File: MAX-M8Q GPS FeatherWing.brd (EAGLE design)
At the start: 50.8 x 22.9 mm, 28 parts, among them Q1 DMG3415U-7, Q2 2N2222, SW1 KMR2, X1 uFL

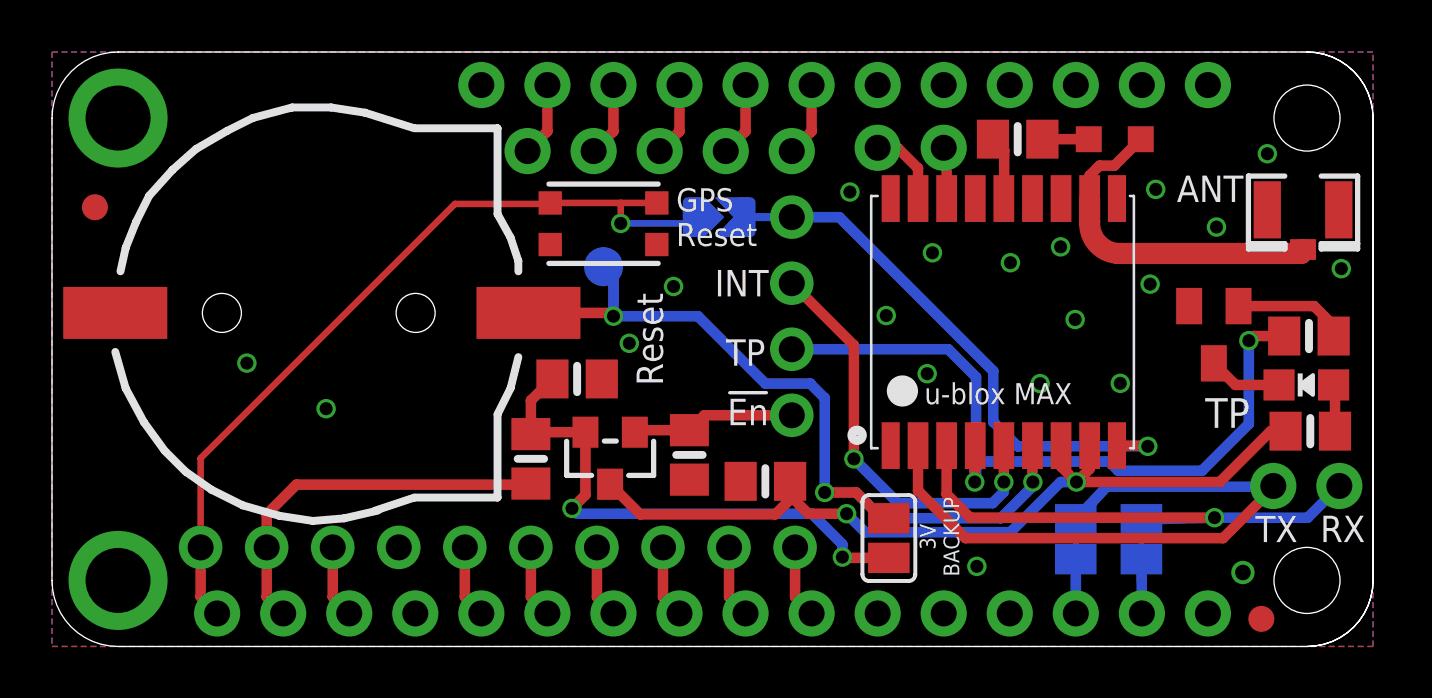
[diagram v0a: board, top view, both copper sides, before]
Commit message: Minor tweaks. Included BOM.
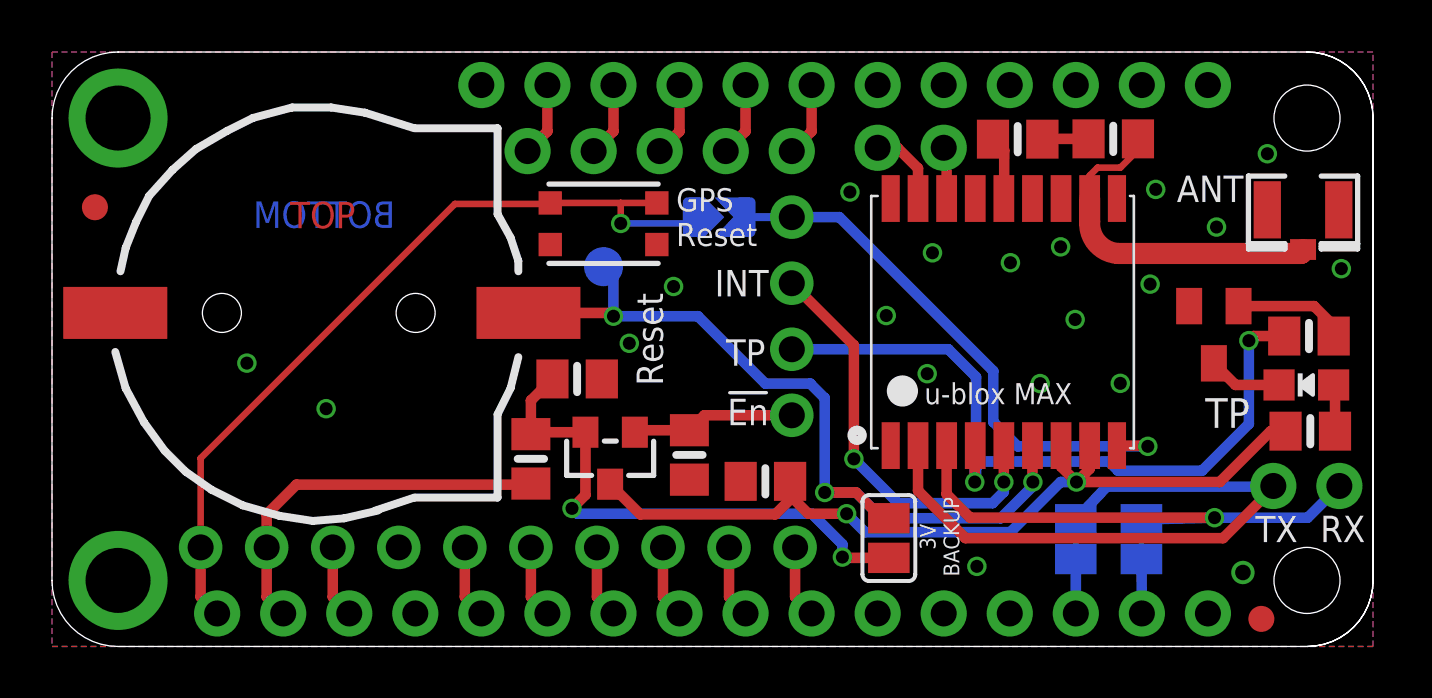
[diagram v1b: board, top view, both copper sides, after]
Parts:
- L1: value (none) -> 33nH; device eagle-ltspice:L2012C -> microbuilder:0805-NO
- moved L1 0.06 mm to (40.8, 19.5), turned to 0 degrees
- renumbered U$12 to U1
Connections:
- net ANT: now also L1.2; no longer L1.1
- net N$4: now also L1.1; no longer L1.2
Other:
- board text added: "B1"
- board text added: "BOTTOM"
- board text added: "C1"
- board text added: "C2"
- board text added: "FB1"
- board text added: "GRESET"
- board text added: "JP3"
- board text added: "L1"
- board text added: "LED1"
- board text added: "Q1"
- board text added: "Q2"
- board text added: "R1"
- board text added: "R2"
- board text added: "R3"
- board text added: "R4"
- board text added: "SW1"
- board text added: "TOP"
- board text added: "U1"
- board text added: "X1"
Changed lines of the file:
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@@
 <text x="34.129728125" y="4.219703125" size="0.6096" layer="21" font="vector" ratio="16" rot="R90" align="center">3V
 BACKUP</text>
+<text x="9.15568125" y="16.082009375" size="1.016" layer="1" ratio="15">TOP</text>
+<text x="13.188946875" y="16.099021875" size="1.016" layer="16" ratio="15" rot="MR0">BOTTOM</text>
+<text x="9.070596875" y="13.18895" size="1.27" layer="51" ratio="12">B1</text>
+<text x="19.842990625" y="13.427203125" size="1.27" layer="51" ratio="12">SW1</text>
+<text x="19.281396875" y="11.16380625" size="1.27" layer="51" ratio="12">C2</text>
+<text x="17.494503125" y="5.701034375" size="1.27" layer="51" ratio="12" rot="R90">FB1</text>
+<text x="20.43861875" y="4.5267875" size="1.27" layer="51" ratio="12">Q1</text>
+<text x="25.118571875" y="8.7302375" size="1.27" layer="51" ratio="12" rot="R90">R2</text>
+<text x="26.616153125" y="4.1013375" size="1.27" layer="51" ratio="12">C1</text>
+<text x="35.567621875" y="12.031728125" size="1.27" layer="51" ratio="12">U1</text>
+<text x="36.1122" y="17.2902875" size="1.27" layer="51" ratio="12">R4</text>
+<text x="40.026334375" y="17.358359375" size="1.27" layer="51" ratio="12">L1</text>
+<text x="43.6681875" y="13.5293125" size="1.27" layer="51" ratio="12">Q2</text>
+<text x="47.190915625" y="16.11605" size="1.27" layer="51" ratio="12">X1</text>
+<text x="47.310040625" y="12.86560625" size="1.27" layer="51" ratio="12">R3</text>
+<text x="43.37888125" y="9.17270625" size="1.016" layer="51" ratio="12">LED1</text>
+<text x="45.046646875" y="7.470903125" size="1.27" layer="51" ratio="12">R1</text>
+<text x="46.57826875" y="4.305559375" size="1.27" layer="51" ratio="12">JP3</text>
+<text x="25.57958125" y="14.89430625" size="0.6096" layer="22" font="vector" ratio="14" rot="MR0" align="center">GRESET</text>
 </plain>
 <attributes>
@@
 <attribute name="VALUE" x="20.066" y="13.97" size="0.4064" layer="28" ratio="10" rot="MR0"/>
 </element>
-<element name="U$12" library="ubloxLib" package="MAX-M8" value="MAX-M8" x="36.6522" y="12.6746" rot="R270"/>
+<element name="U1" library="ubloxLib" package="MAX-M8" value="MAX-M8" x="36.6522" y="12.6746" rot="R270"/>
 <element name="Q2" library="transistor" package="SOT23-BEC" value="2N2222" x="44.6786" y="11.9888" smashed="yes" rot="R180"/>
 <element name="R3" library="microbuilder" package="0805-NO" value="1K" x="48.3362" y="11.938" smashed="yes"/>
 <element name="R4" library="microbuilder" package="0805-NO" value="10 ohm" x="37.1348" y="19.5072" smashed="yes" rot="R180"/>
-<element name="L1" library="eagle-ltspice" package="L2012C" value="" x="40.8686" y="19.5072" smashed="yes" rot="R180">
-<attribute name="SPICEMODEL" value="NONE" x="40.8686" y="19.5072" size="0.0508" layer="27" rot="R180" display="off"/>
-<attribute name="SPICEPREFIX" value="L" x="40.8686" y="19.5072" size="0.0508" layer="27" rot="R180" display="off"/>
-<attribute name="VALUE" x="42.7736" y="22.0472" size="1.27" layer="27" rot="R180"/>
-</element>
 <element name="JP5" library="microbuilder" package="1X02_ROUND" value="" x="33.02" y="19.177" smashed="yes">
 <attribute name="VALUE" x="30.48" y="16.002" size="0.4064" layer="27" ratio="10"/>
@@
 <attribute name="VALUE" x="32.181040625" y="3.769315625" size="0.02" layer="27" rot="R270"/>
 </element>
+<element name="L1" library="microbuilder" package="0805-NO" value="33nH" x="40.8091625" y="19.51964375" smashed="yes"/>
 </elements>
 <signals>
@@
 <via x="10.541" y="9.144" extent="1-16" drill="0.5"/>
 <contactref element="Q2" pad="E"/>
-<contactref element="U$12" pad="10_GND"/>
-<contactref element="U$12" pad="12_GND"/>
-<contactref element="U$12" pad="1_GND"/>
+<contactref element="U1" pad="10_GND"/>
+<contactref element="U1" pad="12_GND"/>
+<contactref element="U1" pad="1_GND"/>
 <via x="45.7962" y="2.8448" extent="1-16" drill="0.6"/>
 <via x="30.6832" y="17.4752" extent="1-16" drill="0.5"/>
@@
 <via x="21.59" y="12.7" extent="1-16" drill="0.5"/>
 <contactref element="TP1" pad="P$1"/>
-<contactref element="U$12" pad="6_V_BCKP"/>
+<contactref element="U1" pad="6_V_BCKP"/>
 <wire x1="21.209" y1="14.605" x2="21.59" y2="14.224" width="0.4064" layer="16"/>
 <wire x1="21.59" y1="14.224" x2="21.59" y2="12.7" width="0.4064" layer="16"/>
@@
 <contactref element="JP3" pad="2"/>
 <contactref element="SJ2" pad="1"/>
-<contactref element="U$12" pad="2_TXD"/>
+<contactref element="U1" pad="2_TXD"/>
 <wire x1="46.9392" y1="6.1468" x2="40.5638" y2="6.1468" width="0.4064" layer="16"/>
 <wire x1="40.5638" y1="6.1468" x2="39.37" y2="4.884928125" width="0.4064" layer="16"/>
@@
 <contactref element="JP3" pad="1"/>
 <contactref element="SJ3" pad="1"/>
-<contactref element="U$12" pad="3_RXD"/>
+<contactref element="U1" pad="3_RXD"/>
 <wire x1="41.89298125" y1="4.884928125" x2="44.704" y2="4.953" width="0.4064" layer="16"/>
 <wire x1="44.704" y1="4.953" x2="48.2854" y2="4.953" width="0.4064" layer="16"/>
@@
 <signal name="ANT">
 <contactref element="X1" pad="3"/>
-<contactref element="U$12" pad="11_RF_IN"/>
-<contactref element="L1" pad="1"/>
+<contactref element="U1" pad="11_RF_IN"/>
 <wire x1="39.9022" y1="17.2246" x2="39.9022" y2="16.3334" width="0.8128" layer="1"/>
 <wire x1="39.9022" y1="16.3334" x2="40.9956" y2="15.113" width="0.8128" layer="1" curve="90"/>
 <wire x1="40.9956" y1="15.113" x2="48.0324" y2="15.113" width="0.8128" layer="1"/>
 <wire x1="48.0324" y1="15.113" x2="48.1076" y2="15.2644" width="0.8128" layer="1" curve="90"/>
-<wire x1="39.9022" y1="17.2246" x2="39.9022" y2="18.109" width="0.4064" layer="1"/>
-<wire x1="39.9022" y1="18.109" x2="40.2844" y2="18.4912" width="0.4064" layer="1"/>
-<wire x1="40.2844" y1="18.4912" x2="40.8526" y2="18.4912" width="0.4064" layer="1"/>
-<wire x1="40.8526" y1="18.4912" x2="41.8686" y2="19.5072" width="0.4064" layer="1"/>
+<wire x1="39.9022" y1="17.2246" x2="39.9022" y2="18.109" width="0.254" layer="1"/>
+<contactref element="L1" pad="2"/>
+<wire x1="39.9022" y1="18.109" x2="40.206675" y2="18.413475" width="0.254" layer="1"/>
+<wire x1="40.206675" y1="18.413475" x2="41.081453125" y2="18.413475" width="0.254" layer="1"/>
+<wire x1="41.081453125" y1="18.413475" x2="41.7591625" y2="19.091184375" width="0.254" layer="1"/>
+<wire x1="41.7591625" y1="19.091184375" x2="41.7591625" y2="19.51964375" width="0.254" layer="1"/>
 </signal>
 <signal name="3V">
@@
 <contactref element="JP1" pad="1"/>
 <wire x1="28.448" y1="16.51" x2="26.67" y2="16.51" width="0.3048" layer="16"/>
-<contactref element="U$12" pad="9_RESET_N"/>
+<contactref element="U1" pad="9_RESET_N"/>
 <wire x1="40.9522" y1="7.7246" x2="42.1102" y2="7.7246" width="0.4064" layer="1"/>
 <wire x1="42.1102" y1="7.7246" x2="42.1386" y2="7.6962" width="0.4064" layer="1"/>
@@
 <wire x1="27.813" y1="5.08" x2="28.382" y2="5.649" width="0.4064" layer="1"/>
 <wire x1="28.382" y1="5.649" x2="28.382" y2="6.35" width="0.4064" layer="1"/>
-<contactref element="U$12" pad="7_VCC_IO"/>
-<contactref element="U$12" pad="8_VCC"/>
+<contactref element="U1" pad="7_VCC_IO"/>
+<contactref element="U1" pad="8_VCC"/>
 <contactref element="R1" pad="2"/>
 <wire x1="28.382" y1="6.35" x2="28.382" y2="5.8064" width="0.4064" layer="1"/>
@@
 <signal name="TP">
 <contactref element="R3" pad="1"/>
-<contactref element="U$12" pad="4_TIMEPULSE"/>
+<contactref element="U1" pad="4_TIMEPULSE"/>
 <contactref element="JP1" pad="3"/>
 <wire x1="47.3862" y1="11.938" x2="46.2026" y2="11.938" width="0.4064" layer="1"/>
@@
 </signal>
 <signal name="EXTINT">
-<contactref element="U$12" pad="5_EXTINT"/>
+<contactref element="U1" pad="5_EXTINT"/>
 <contactref element="JP1" pad="2"/>
 <wire x1="36.6022" y1="7.7246" x2="36.6014" y2="7.7238" width="0.4064" layer="1"/>
@@
 </signal>
 <signal name="VCC_RF">
-<contactref element="U$12" pad="14_VCC_RF"/>
+<contactref element="U1" pad="14_VCC_RF"/>
 <contactref element="R4" pad="2"/>
 <wire x1="36.6022" y1="17.2246" x2="36.6166" y2="17.239" width="0.4064" layer="1"/>
@@
 <wire x1="36.6166" y1="19.0754" x2="36.1848" y2="19.5072" width="0.4064" layer="1"/>
 </signal>
-<signal name="N$4">
-<contactref element="R4" pad="1"/>
-<contactref element="L1" pad="2"/>
-<wire x1="38.0848" y1="19.5072" x2="39.8686" y2="19.5072" width="0.4064" layer="1"/>
-</signal>
 <signal name="SDA">
 <contactref element="JP5" pad="2"/>
-<contactref element="U$12" pad="16_SDA"/>
+<contactref element="U1" pad="16_SDA"/>
 <wire x1="34.4022" y1="17.2246" x2="34.4022" y2="19.014" width="0.4064" layer="1"/>
 <wire x1="34.4022" y1="19.014" x2="34.29" y2="19.177" width="0.4064" layer="1"/>
@@
 <signal name="SCL">
 <contactref element="JP5" pad="1"/>
-<contactref element="U$12" pad="17_SCL"/>
+<contactref element="U1" pad="17_SCL"/>
 <wire x1="33.3022" y1="17.2246" x2="33.3022" y2="18.3868" width="0.4064" layer="1"/>
 <wire x1="33.3022" y1="18.3868" x2="32.512" y2="19.177" width="0.4064" layer="1"/>
 <wire x1="32.512" y1="19.177" x2="31.75" y2="19.177" width="0.4064" layer="1"/>
 </signal>
+<signal name="N$4">
+<contactref element="L1" pad="1"/>
+<contactref element="R4" pad="1"/>
+<wire x1="38.0848" y1="19.5072" x2="38.09724375" y2="19.51964375" width="0.4064" layer="1"/>
+<wire x1="38.09724375" y1="19.51964375" x2="39.8591625" y2="19.51964375" width="0.4064" layer="1"/>
+</signal>
 </signals>
